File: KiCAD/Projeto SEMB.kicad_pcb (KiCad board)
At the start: 2 copper layers, 114 x 39 mm, 61 parts, among them J1 Battery-12V, J2 ST-Link V2, M1 Motor_DC, Q2 IRLML5203, SW1 Reset, SW2 BOOT_0, SW3 SW_SPDT, U1 STM32F411CEUx, U10 XL4015, U11 LCD-016N002L, U13 INA333xxDGK, U2 2SMPP-03, U3 TLV2371P, U4 DRV8212P, U5 PCF8574A, U7 TPS7A2433DBVR, Y1 LSE

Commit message: Footprints
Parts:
- added R11: 1k, Resistor_SMD:R_0603_1608Metric_Pad0.98x0.95mm_HandSolder, F.Cu at (140.8, 99.4)
- added R12: 10k, Resistor_SMD:R_0603_1608Metric_Pad0.98x0.95mm_HandSolder, F.Cu at (140.8, 101.9)
- added SW4: User Button, Button_Switch_SMD:SW_SPST_B3U-1000P-B, F.Cu at (141.6, 96.0)
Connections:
- U1 pad 13: unconnected-(U1-PA3-Pad13) -> PA3
- U13 pad 6: PB14 -> PA3

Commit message: User Interface
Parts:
- added BZ1: Buzzer, Buzzer_Beeper:Buzzer_Mallory_AST1109MLTRQ, F.Cu at (84.2, 77.0)
- added D1: 1N4007, Diode_THT:D_DO-41_SOD81_P10.16mm_Horizontal, F.Cu at (91.6, 83.7)
- added R13: 100R, Resistor_SMD:R_0603_1608Metric_Pad0.98x0.95mm_HandSolder, F.Cu at (95.0, 83.3)
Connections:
- U1 pad 31: unconnected-(U1-PA10-Pad31) -> PA10
- U1 pad 5: PH0 -> unconnected-(U1-PH0-Pad5)
- U1 pad 6: PH1 -> unconnected-(U1-PH1-Pad6)
- U5 pad 13: unconnected-(U5-~{INT}-Pad13) -> +5V
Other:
- board size 114 x 39 mm -> 153 x 122.5 mm

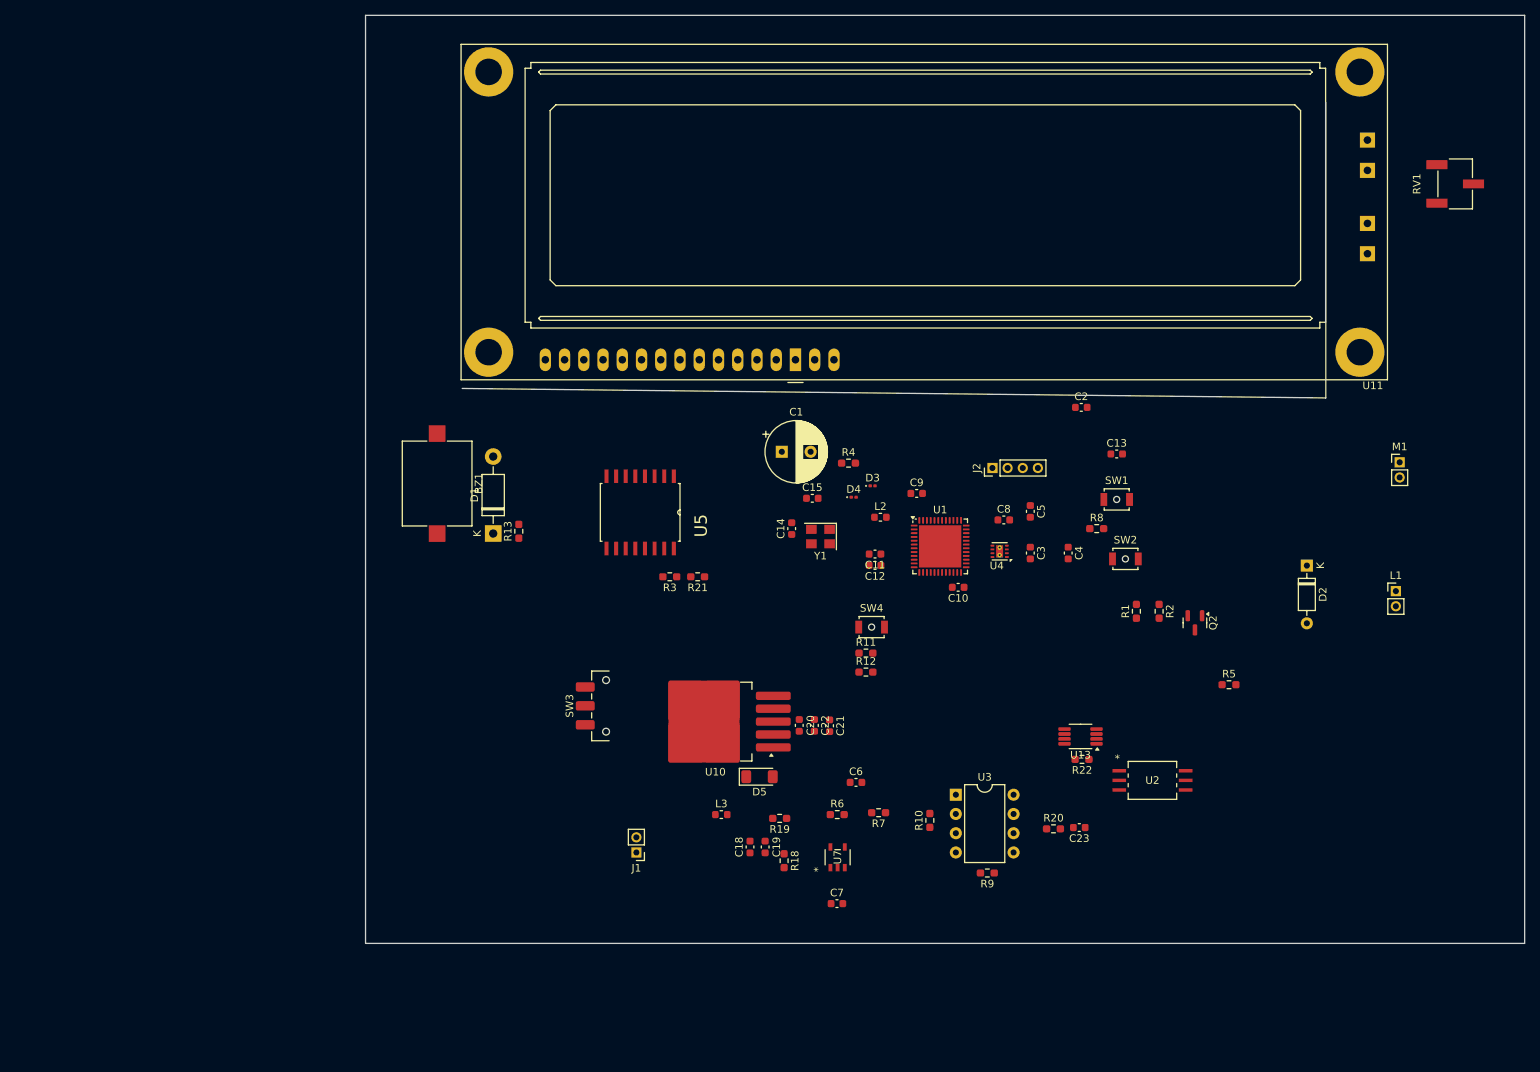
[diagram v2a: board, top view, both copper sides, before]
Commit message: Atualizando esquemático
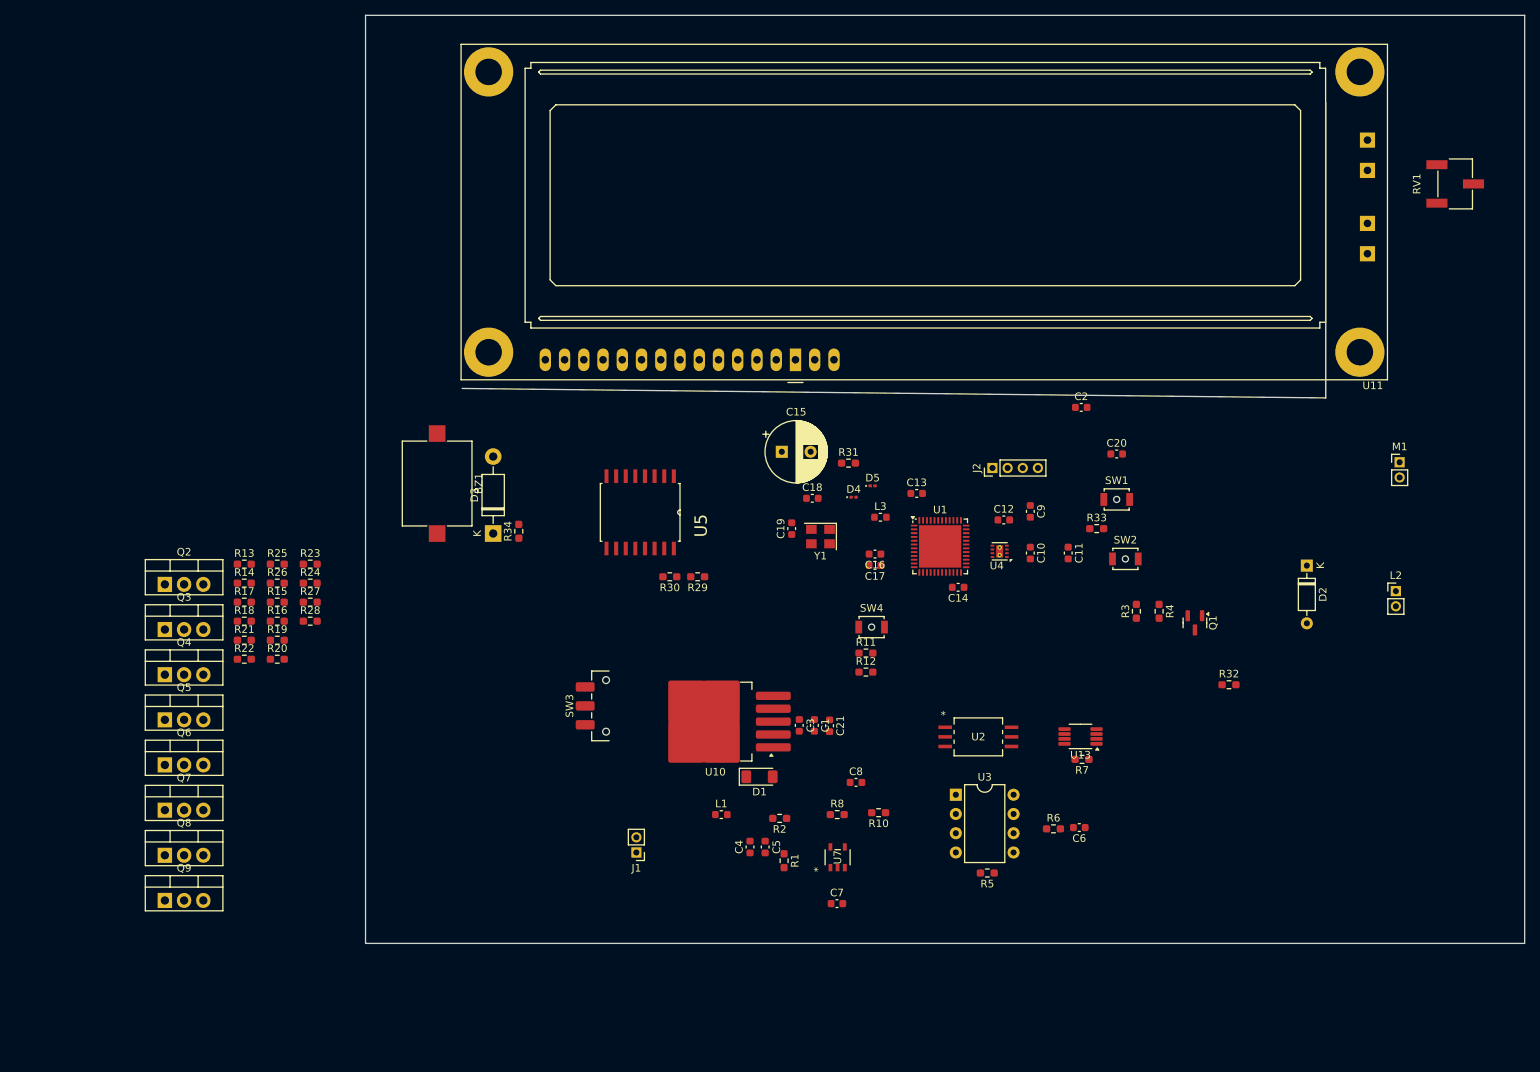
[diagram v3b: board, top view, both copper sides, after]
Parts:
- removed the R10 at (149.2, 121.5)
- added Q2: IRF740, Package_TO_SOT_THT:TO-220-3_Vertical, F.Cu at (48.3, 90.4)
- added Q3: IRF740, Package_TO_SOT_THT:TO-220-3_Vertical, F.Cu at (48.3, 96.3)
- added Q4: IRF740, Package_TO_SOT_THT:TO-220-3_Vertical, F.Cu at (48.3, 102.3)
- added Q5: IRF740, Package_TO_SOT_THT:TO-220-3_Vertical, F.Cu at (48.3, 108.2)
- added Q6: IRF740, Package_TO_SOT_THT:TO-220-3_Vertical, F.Cu at (48.3, 114.2)
- added Q7: IRF740, Package_TO_SOT_THT:TO-220-3_Vertical, F.Cu at (48.3, 120.2)
- added Q8: IRF740, Package_TO_SOT_THT:TO-220-3_Vertical, F.Cu at (48.3, 126.1)
- added Q9: IRF740, Package_TO_SOT_THT:TO-220-3_Vertical, F.Cu at (48.3, 132.1)
- added R13: 10k, Resistor_SMD:R_0603_1608Metric_Pad0.98x0.95mm_HandSolder, F.Cu at (58.8, 87.7)
- added R14: 10k, Resistor_SMD:R_0603_1608Metric_Pad0.98x0.95mm_HandSolder, F.Cu at (58.8, 90.2)
- added R15: 10k, Resistor_SMD:R_0603_1608Metric_Pad0.98x0.95mm_HandSolder, F.Cu at (63.1, 92.7)
- added R16: 10k, Resistor_SMD:R_0603_1608Metric_Pad0.98x0.95mm_HandSolder, F.Cu at (63.1, 95.2)
- added R17: 10k, Resistor_SMD:R_0603_1608Metric_Pad0.98x0.95mm_HandSolder, F.Cu at (58.8, 92.7)
- added R18: 10k, Resistor_SMD:R_0603_1608Metric_Pad0.98x0.95mm_HandSolder, F.Cu at (58.8, 95.2)
- added R19: 10k, Resistor_SMD:R_0603_1608Metric_Pad0.98x0.95mm_HandSolder, F.Cu at (63.1, 97.7)
- added R20: 10k, Resistor_SMD:R_0603_1608Metric_Pad0.98x0.95mm_HandSolder, F.Cu at (63.1, 100.2)
- added R21: 10k, Resistor_SMD:R_0603_1608Metric_Pad0.98x0.95mm_HandSolder, F.Cu at (58.8, 97.7)
- added R22: 10k, Resistor_SMD:R_0603_1608Metric_Pad0.98x0.95mm_HandSolder, F.Cu at (58.8, 100.2)
- added R23: 10k, Resistor_SMD:R_0603_1608Metric_Pad0.98x0.95mm_HandSolder, F.Cu at (67.5, 87.7)
- added R24: 10k, Resistor_SMD:R_0603_1608Metric_Pad0.98x0.95mm_HandSolder, F.Cu at (67.5, 90.2)
- added R25: 10k, Resistor_SMD:R_0603_1608Metric_Pad0.98x0.95mm_HandSolder, F.Cu at (63.1, 87.7)
- added R26: 10k, Resistor_SMD:R_0603_1608Metric_Pad0.98x0.95mm_HandSolder, F.Cu at (63.1, 90.2)
- added R27: 10k, Resistor_SMD:R_0603_1608Metric_Pad0.98x0.95mm_HandSolder, F.Cu at (67.5, 92.7)
- added R28: 10k, Resistor_SMD:R_0603_1608Metric_Pad0.98x0.95mm_HandSolder, F.Cu at (67.5, 95.2)
- R5: renamed from R9; value 40k -> 1K
- moved U2 23.7 mm to (155.6, 110.5)
- renumbered C22 to C1, C3 to C10, C4 to C11, C8 to C12, C9 to C13, C10 to C14, C1 to C15, C11 to C16, C12 to C17, C15 to C18, C14 to C19, C13 to C20, C20 to C3, C18 to C4, C19 to C5, C23 to C6, C6 to C8, C5 to C9, D5 to D1, D1 to D3, D3 to D5, L3 to L1, L1 to L2, L2 to L3, Q2 to Q1, R18 to R1, R7 to R10, R19 to R2, R21 to R29, R1 to R3, R3 to R30, R4 to R31, R5 to R32, R8 to R33, R13 to R34, R2 to R4, R20 to R6, R22 to R7, R6 to R8
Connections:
- R29 pad 1: +5V -> +3.3V
- R30 pad 1: +5V -> +3.3V
- R5 pad 1: +5V -> +3.3V
- RV1 pad 3: 3.3V -> +5V
- U11 pad 10: Net-(U11-DB3) -> DB3
- U11 pad 11: Net-(U11-DB4) -> DB4
- U11 pad 12: Net-(U11-DB5) -> DB5
- U11 pad 13: Net-(U11-DB6) -> DB6
- U11 pad 14: Net-(U11-DB7) -> DB7
- U11 pad 7: Net-(U11-DB0) -> DB0
- U11 pad 8: Net-(U11-DB1) -> DB1
- U11 pad 9: Net-(U11-DB2) -> DB2
- U13 pad 7: +5V -> +3.3V
- U3 pad 7: +5V -> +3.3V
- U4 pad 7: 3.3V -> +3.3V
- U5 pad 10: Net-(U11-DB5) -> P5
- U5 pad 11: Net-(U11-DB6) -> P6
- U5 pad 12: Net-(U11-DB7) -> P7
- U5 pad 16: +5V -> +3.3V
- U5 pad 4: Net-(U11-DB0) -> P0
- U5 pad 5: Net-(U11-DB1) -> P1
- U5 pad 6: Net-(U11-DB2) -> P2
- U5 pad 7: Net-(U11-DB3) -> P3
- U5 pad 9: Net-(U11-DB4) -> P4

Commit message: .
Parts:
- added C22: 0.1uF, Capacitor_SMD:C_0603_1608Metric, F.Cu at (191.3, 93.4)
- moved BZ1 125.5 mm to (208.1, 57.2)
- moved D3 111.7 mm to (201.1, 61.9)
- moved R34 108.7 mm to (202.1, 64.8), turned to 0 degrees
- moved Q2 90.9 mm to (139.2, 92.8), turned to 180 degrees
- moved Q9 86.8 mm to (125.7, 92.8), turned to 180 degrees
- moved U10 83.0 mm to (39.7, 125.4)
- moved C21 80.1 mm to (57.1, 122.7)
- moved C3 79.1 mm to (54.1, 122.7), turned to -90 degrees
- moved R13 78.6 mm to (136.6, 98.2)
- moved C1 76.1 mm to (59.1, 122.7)
- moved SW3 76.1 mm to (37.6, 138.7)
- moved R1 72.2 mm to (57.8, 126.8)
- moved R2 72.2 mm to (57.8, 130.4), turned to -90 degrees
- moved R10 70.3 mm to (72.6, 127.9), turned to -90 degrees
- moved U7 69.4 mm to (67.7, 128.3)
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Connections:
- C6 pad 1: GND -> Net-(U13-V-)
- U13 pad 4: GND -> Net-(U13-V-)
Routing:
- net GND: track 0.00 -> 556.8 mm, vias 0 -> 2
- net +3.3V: track 0.00 -> 474.3 mm, vias 0 -> 5
- net +5V: track 0.00 -> 291.9 mm, vias 0 -> 2
- net +12V: track 0.00 -> 185.9 mm, vias 0 -> 2
- net DB0: track 0.00 -> 133.1 mm, vias 0 -> 1
- net Net-(U11-VO): track 0.00 -> 127.6 mm, vias 0 -> 1
- net DB1: track 0.00 -> 113.5 mm, vias 0 -> 1
- net PA10: track 0.00 -> 103.4 mm, vias 0 -> 2
- net PB7: track 0.00 -> 89.1 mm
- net DB2: track 0.00 -> 88.5 mm, vias 0 -> 1
- net PB5: track 0.00 -> 74.8 mm, vias 0 -> 2
- net PA9: track 0.00 -> 73.0 mm
- net DB3: track 0.00 -> 67.6 mm
- net PA3: track 0.00 -> 65.3 mm, vias 0 -> 2
- net PA8: track 0.00 -> 60.5 mm
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- added copper zone on F.Cu, net GND
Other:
- board size 153 x 122.5 mm -> 185.5 x 112 mm

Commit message: substitute
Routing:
- net +5V: track 291.9 -> 376.0 mm
- net PB6: track 8.02 -> 71.3 mm, vias 0 -> 2
- net +3.3V: track 474.3 -> 467.7 mm, vias 5 -> 7
- net PB5: track 74.8 -> 77.2 mm
- net Net-(D4-A): track 1.52 -> 2.49 mm
- net PB7: track 89.1 -> 89.7 mm
- net +12V: vias 2 -> 1
- removed copper zone on F.Cu, net GND
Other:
- board size 185.5 x 112 mm -> 189.2 x 118.2 mm
